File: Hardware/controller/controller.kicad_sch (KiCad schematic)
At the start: 39 parts, among them J101 Conn_02x10_Odd_Even, J102 Conn_02x10_Odd_Even, J103 Conn_02x10_Odd_Even, M101 Fan_4pin, Q101 MMBT3904, U101 PCA9543A, U102 EMC2101-R

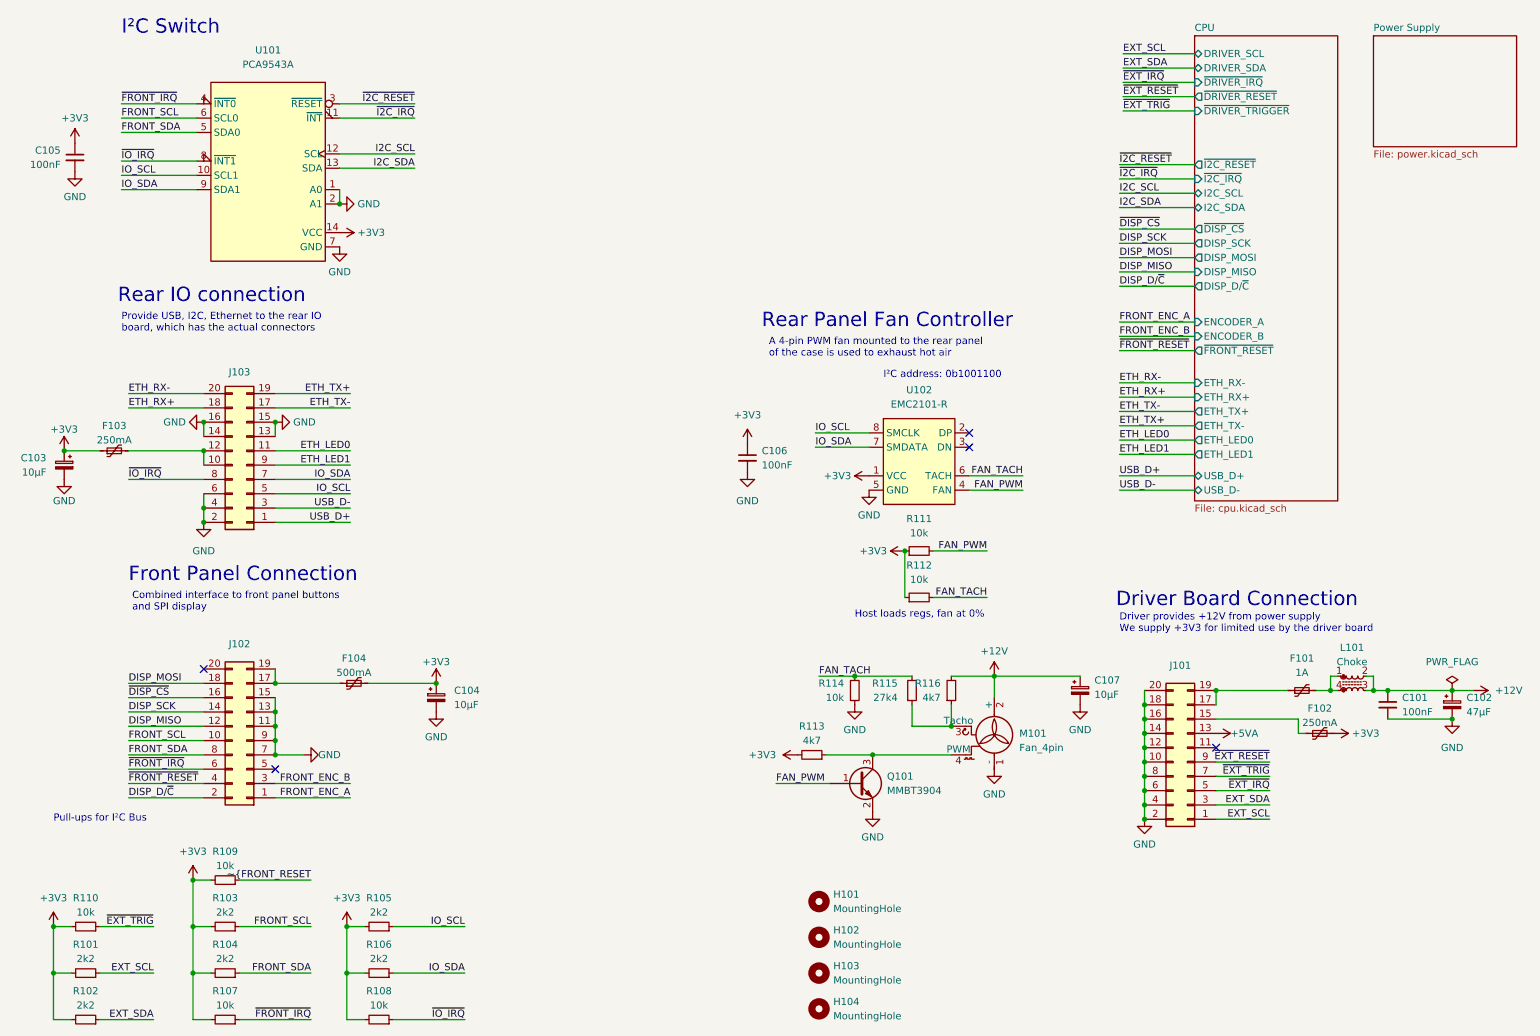
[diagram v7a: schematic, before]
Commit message: Driver input protection; heatsink footprint tweaks
- Updated the footprint for the heatsink on the driver board to include
  a 3D model. Also fixed it… the distances were kind of out of whack and
  it would never have really fit

- Added a reverse polarity protection diode to the input; it gets its
  own cute little heatsink

- Minor movement to better accomodate a fan. A 20mm fan will likely
  interfere with the input connector (it might be worth switching to a
  different kind, or just soldering the connections altogether: spade
  terminals seem like a good choice for high current) and be very tight
  against the input diode's heatsink. We'll try with a 10mm fan and see
  if that's enough airflow.
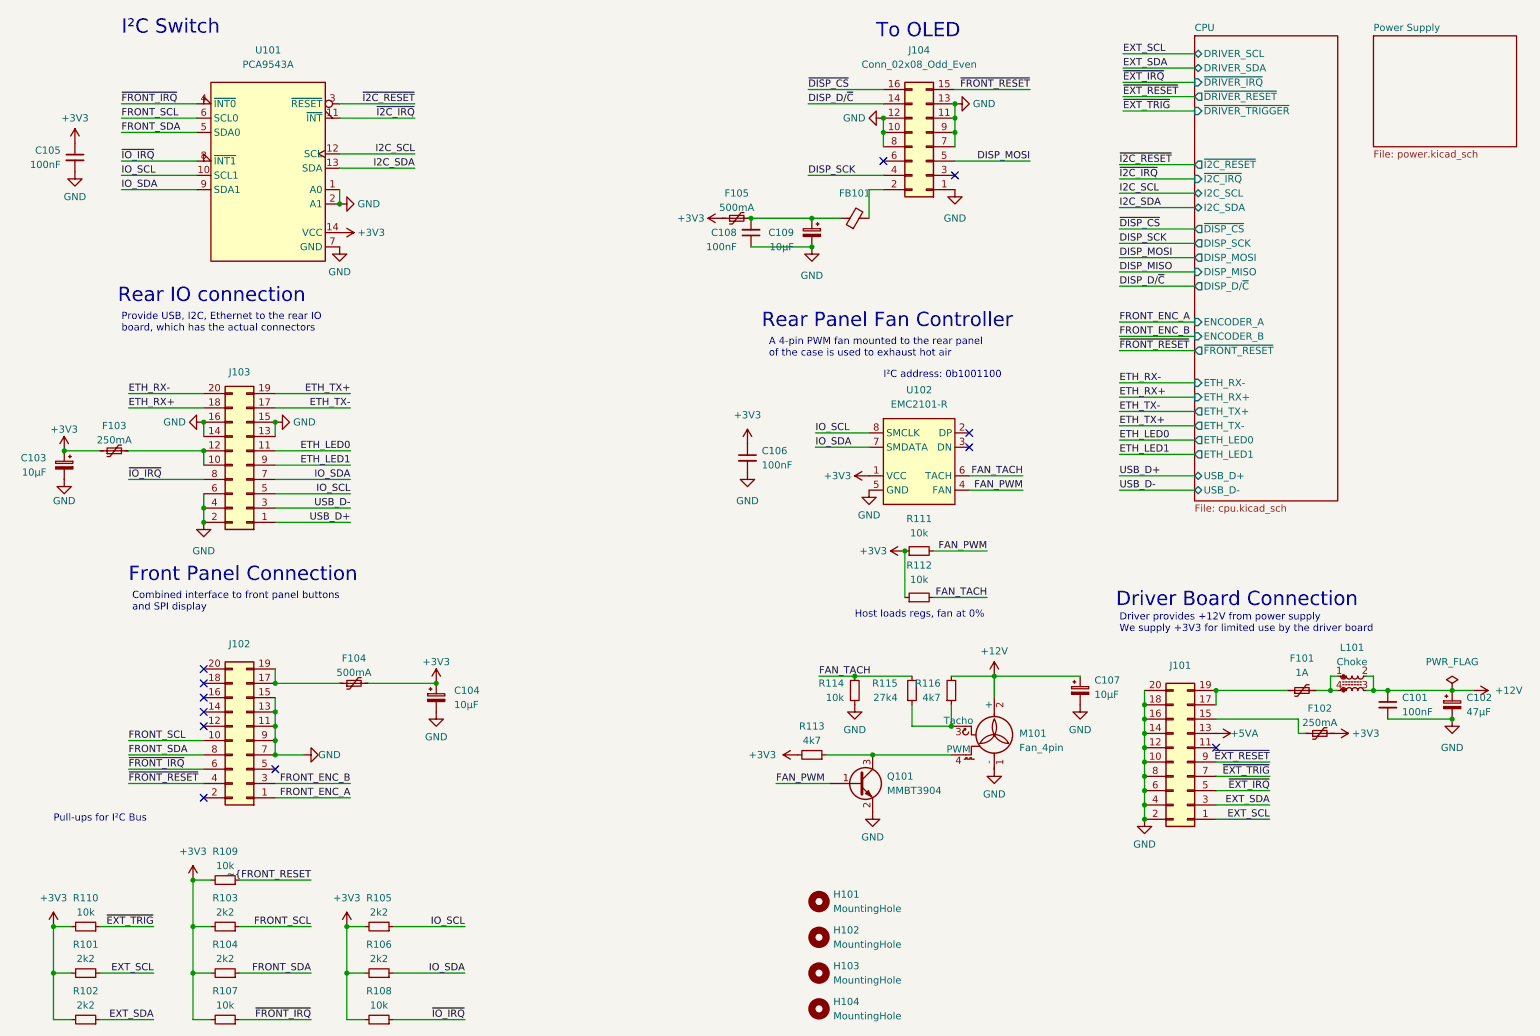
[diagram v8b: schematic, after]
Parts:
- added C108: 100nF, Capacitor_SMD:C_0805_2012Metric_Pad1.18x1.45mm_HandSolder, symbol Device:C_Small
- added C109: 10µF, Capacitor_Tantalum_SMD:CP_EIA-3216-18_Kemet-A_Pad1.58x1.35mm_HandSolder, symbol Device:C_Polarized_Small
- added F105: 500mA, Fuse:Fuse_1206_3216Metric_Pad1.42x1.75mm_HandSolder, symbol Device:Polyfuse_Small
- added FB101: FerriteBead_Small, Inductor_SMD:L_0805_2012Metric_Pad1.05x1.20mm_HandSolder, symbol Device:FerriteBead_Small
- added J104: Conn_02x08_Odd_Even, Connector_IDC:IDC-Header_2x08-1MP_P2.54mm_Latch_Vertical, symbol Connector_Generic:Conn_02x08_Odd_Even
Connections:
- net +3V3: now also F105.1
- net DISP_D/~{C}: now also J104.14 (Pin_14); no longer J102.2 (Pin_2)
- net DISP_MISO: no longer J102.12 (Pin_12)
- net DISP_MOSI: now also J104.5 (Pin_5); no longer J102.18 (Pin_18)
- net DISP_SCK: now also J104.4 (Pin_4); no longer J102.14 (Pin_14)
- net GND: now also C108.1, C109.2, J104.1 (Pin_1), J104.10 (Pin_10), J104.11 (Pin_11), J104.12 (Pin_12), J104.13 (Pin_13), J104.7 (Pin_7), J104.8 (Pin_8), J104.9 (Pin_9)
- net ~{DISP_CS}: now also J104.16 (Pin_16); no longer J102.16 (Pin_16)
- net ~{FRONT_RESET}: now also J104.15 (Pin_15)
- new net: C108.2, C109.1, F105.2, FB101.1
- new net: FB101.2, J104.2 (Pin_2)
- no-connect marks 5 -> 12
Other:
- note added: "To OLED"
